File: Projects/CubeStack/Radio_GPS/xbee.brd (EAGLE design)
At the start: 63.5 x 76.2 mm, 78 parts, among them Q1 310mA/60V/1.6Ω, Q2 310mA/60V/1.6Ω, Q3 310mA/60V/1.6Ω, Q4 310mA/60V/1.6Ω, U1 TS3USB221A, U2 V_REG_MIC5216, U3 TS3USB221A, U4 V_REG_MIC5216, U5 Value, U6 TPS62130_RGT_16

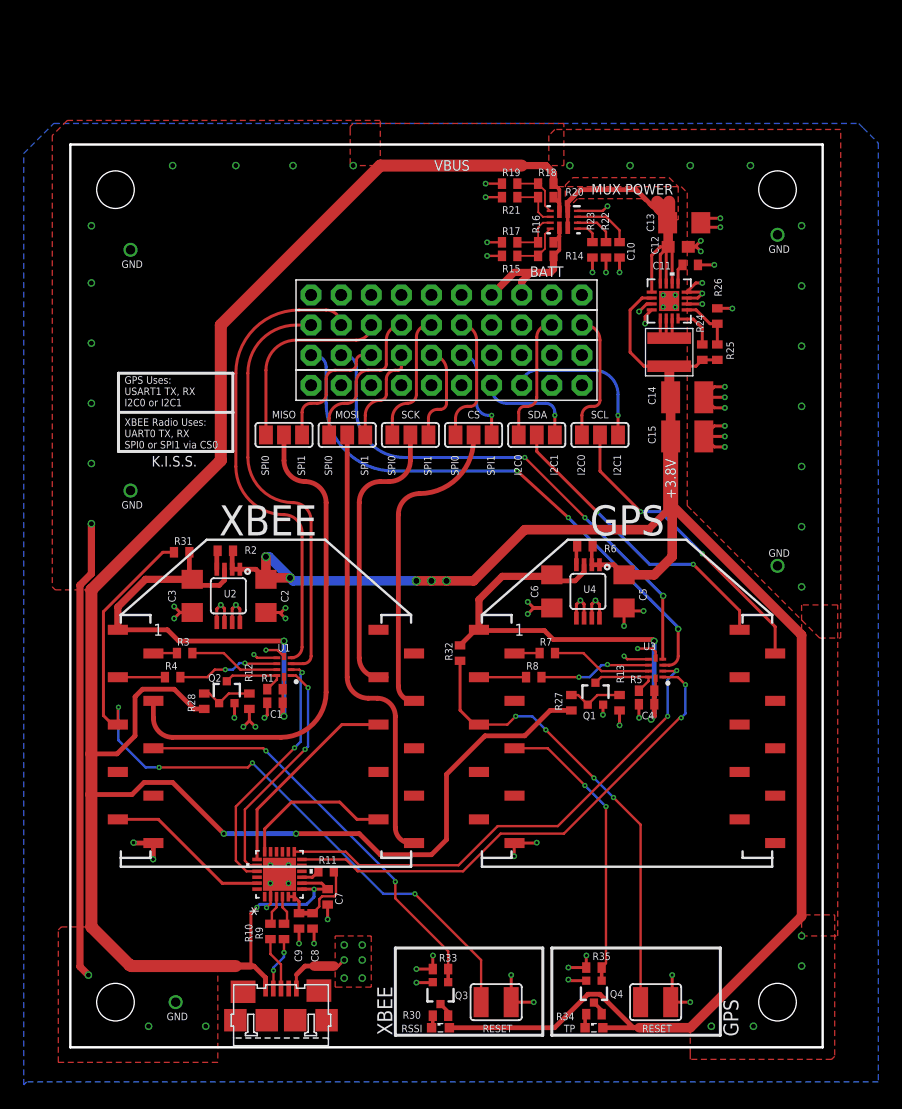
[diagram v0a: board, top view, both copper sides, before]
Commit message: Added some part values
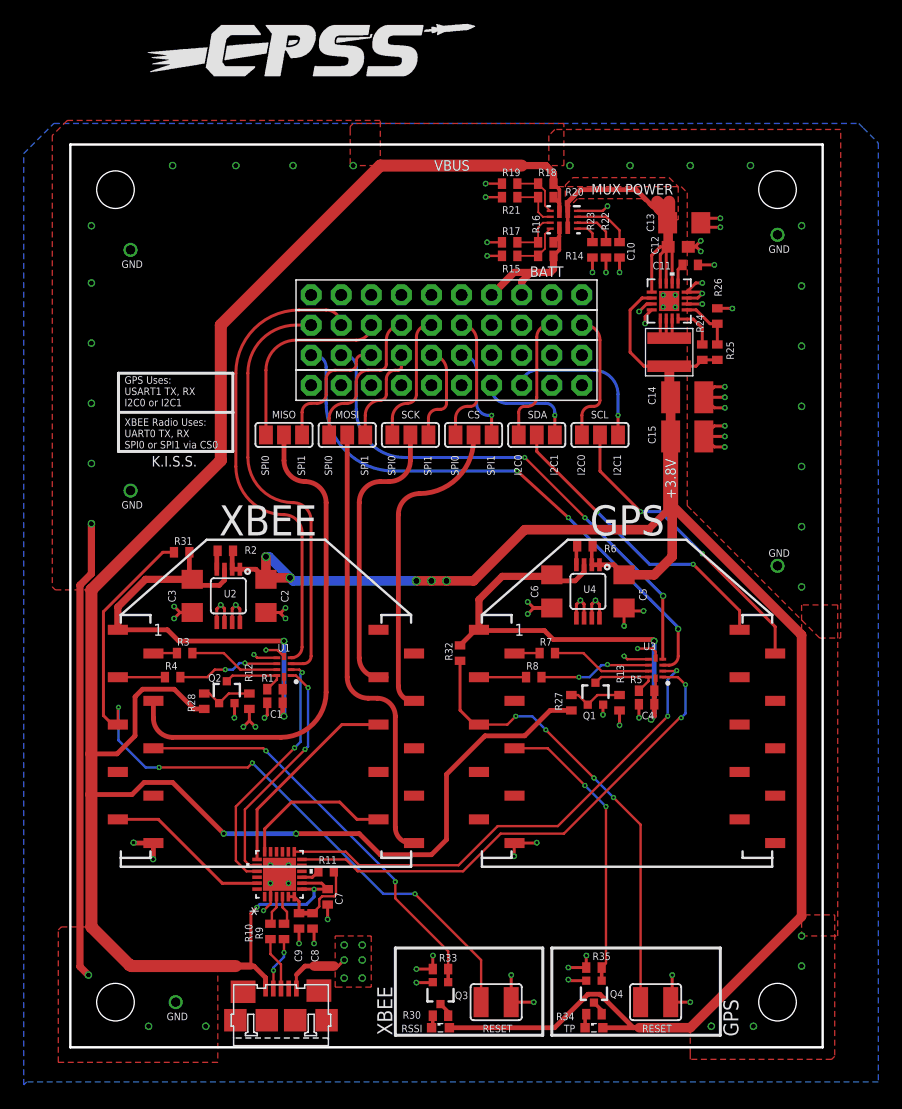
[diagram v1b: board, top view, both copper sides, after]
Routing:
- net GND: track 158.3 -> 160.4 mm
- net N$28: track 5.63 -> 7.65 mm
